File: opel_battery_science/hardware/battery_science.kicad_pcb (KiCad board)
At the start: 2 copper layers, 61 x 44.5 mm, 49 parts, among them P201 CONN_01X06, P301 CONN_01X08, P401 CONN_01X05, P402 CONN_01X05, Q301 BSS84, SW201 SPST, SW202 SPST, U201 LPC11C14, U301 BQ76925, U401 ADS1148IPWR

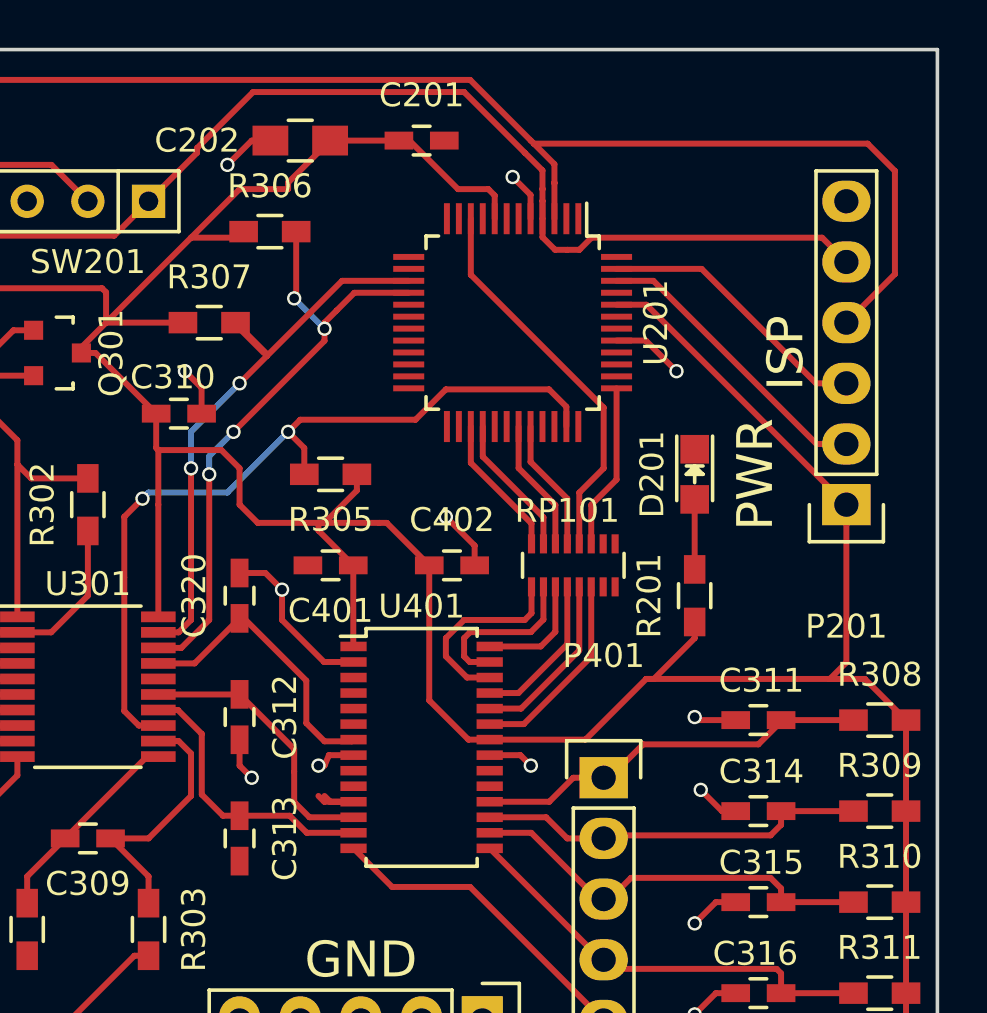
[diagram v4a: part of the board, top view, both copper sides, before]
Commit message: Moved input pins for ease of programming and avoiding accidental negative readings
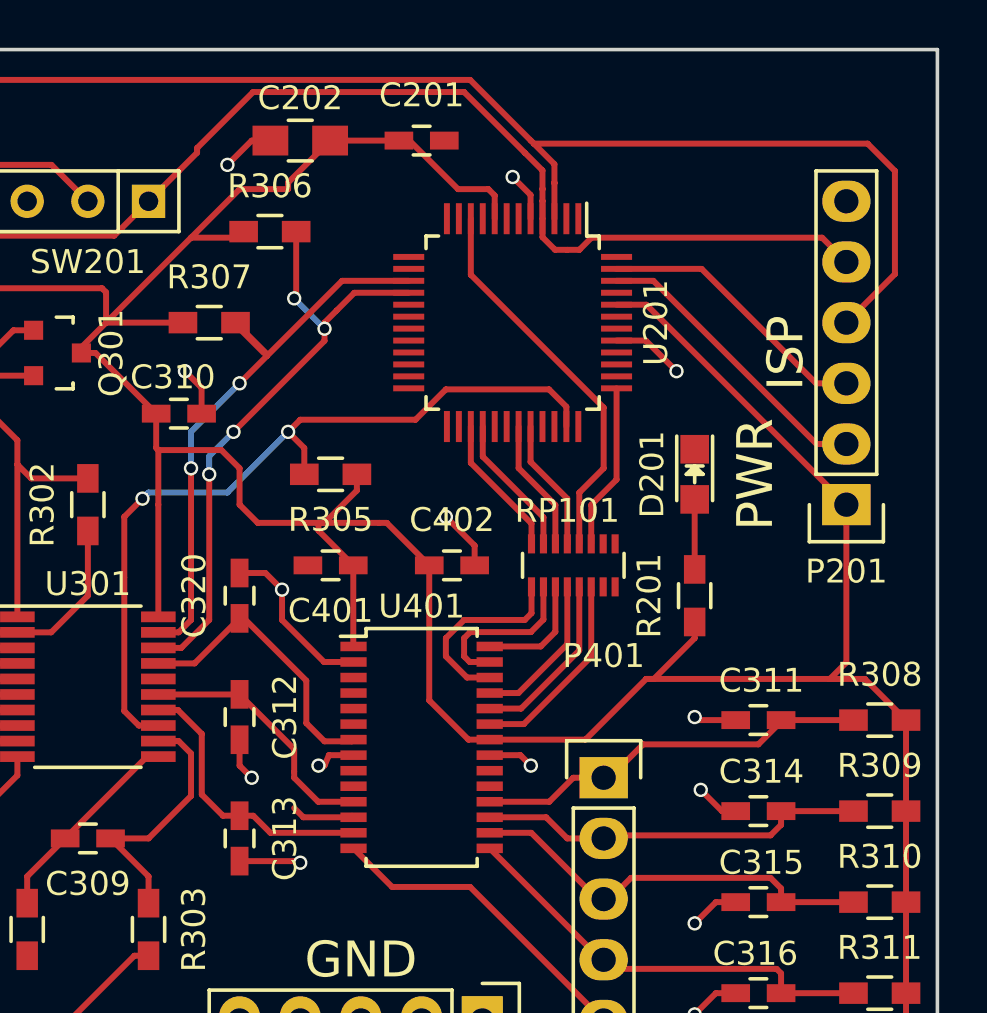
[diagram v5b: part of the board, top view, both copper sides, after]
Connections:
- U401 pad 11: GND -> /ADC/Thermistors/VCOUT
- U401 pad 12: /ADC/Thermistors/VCOUT -> GND
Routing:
- net GND: track 67.0 -> 69.4 mm, vias 24 -> 25
- net /ADC/Thermistors/VCOUT: track 11.7 -> 10.8 mm
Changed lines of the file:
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@@
     (thickness 1.6)
     (drawings 10)
-    (tracks 490)
+    (tracks 492)
     (zones 0)
     (modules 49)
@@
     (tags "capacitor 0805")
     (attr smd)
-    (fp_text reference C202 (at 4.318 0 180) (layer F.SilkS)
+    (fp_text reference C202 (at 0 1.778 180) (layer F.SilkS)
       (effects (font (size 1 1) (thickness 0.15)))
     )
@@
     (descr "Through hole pin header")
     (tags "pin header")
-    (fp_text reference P201 (at 0 -5.1 180) (layer F.SilkS)
+    (fp_text reference P201 (at 0 -2.794 180) (layer F.SilkS)
       (effects (font (size 1 1) (thickness 0.15)))
     )
@@
       (net 81 "Net-(U401-Pad10)"))
     (pad 11 smd rect (at -2.85 2.275) (size 1.1 0.4) (layers F.Cu F.Paste F.Mask)
-      (net 1 GND))
+      (net 21 /ADC/Thermistors/VCOUT))
     (pad 12 smd rect (at -2.85 2.925) (size 1.1 0.4) (layers F.Cu F.Paste F.Mask)
-      (net 21 /ADC/Thermistors/VCOUT))
+      (net 1 GND))
     (pad 13 smd rect (at -2.85 3.575) (size 1.1 0.4) (layers F.Cu F.Paste F.Mask)
       (net 22 /ADC/Thermistors/VIOUT))
@@
     (effects (font (size 1.5 1.5) (thickness 0.3)))
   )
-  (segment (start 158.44 129.275) (end 157.215 129.275) (width 0.25) (layer F.Cu) (net 1) (status 400000))
-  (segment (start 157.215 129.275) (end 156.972 129.032) (width 0.25) (layer F.Cu) (net 1))
-  (segment (start 158.44 129.275) (end 157.469 129.275) (width 0.25) (layer F.Cu) (net 1) (status 400000))
-  (segment (start 157.469 129.275) (end 157.226 129.032) (width 0.25) (layer F.Cu) (net 1))
+  (segment (start 158.44 129.925) (end 156.341 129.925) (width 0.25) (layer F.Cu) (net 1) (status 400000))
+  (segment (start 156.341 129.925) (end 155.956 129.54) (width 0.25) (layer F.Cu) (net 1))
+  (segment (start 153.67 131.76) (end 156.144 131.76) (width 0.25) (layer F.Cu) (net 1))
+  (via (at 156.21 131.826) (size 0.6) (drill 0.4) (layers F.Cu B.Cu) (net 1))
+  (segment (start 156.144 131.76) (end 156.21 131.826) (width 0.25) (layer F.Cu) (net 1))
   (segment (start 163.51 119.38) (end 163.51 118.552) (width 0.25) (layer F.Cu) (net 1))
   (via (at 162.306 117.348) (size 0.6) (drill 0.4) (layers F.Cu B.Cu) (net 1))
@@
   (segment (start 136.398 114.808) (end 135.382 114.808) (width 0.25) (layer F.Cu) (net 1))
   (segment (start 137.094 115.504) (end 136.398 114.808) (width 0.25) (layer F.Cu) (net 1))
+  (segment (start 158.375 129.86) (end 158.44 129.925) (width 0.25) (layer F.Cu) (net 1))
   (segment (start 161.61 119.38) (end 161.61 125.034) (width 0.25) (layer F.Cu) (net 2))
   (segment (start 163.251 126.675) (end 164.14 126.675) (width 0.25) (layer F.Cu) (net 2))
@@
   (segment (start 179.367 125.857) (end 176.337 125.857) (width 0.25) (layer F.Cu) (net 20))
   (segment (start 170.561 126.873) (end 169.037 128.397) (width 0.25) (layer F.Cu) (net 20))
-  (segment (start 155.956 128.016) (end 155.956 129.286) (width 0.25) (layer F.Cu) (net 21))
+  (segment (start 155.956 128.016) (end 155.956 128.27) (width 0.25) (layer F.Cu) (net 21))
+  (segment (start 153.67 124.78) (end 155.956 127.066) (width 0.25) (layer F.Cu) (net 21))
   (segment (start 155.956 128.016) (end 155.956 127.066) (width 0.25) (layer F.Cu) (net 21))
-  (segment (start 153.67 124.78) (end 155.956 127.066) (width 0.25) (layer F.Cu) (net 21))
-  (segment (start 156.595 129.925) (end 158.44 129.925) (width 0.25) (layer F.Cu) (net 21) (status 800000))
-  (segment (start 155.956 129.286) (end 156.595 129.925) (width 0.25) (layer F.Cu) (net 21))
+  (segment (start 156.961 129.275) (end 158.44 129.275) (width 0.25) (layer F.Cu) (net 21))
+  (segment (start 155.956 128.27) (end 156.961 129.275) (width 0.25) (layer F.Cu) (net 21))
   (segment (start 150.27 124.785) (end 153.741 124.785) (width 0.25) (layer F.Cu) (net 21))
-  (segment (start 153.67 129.86) (end 155.768 129.86) (width 0.25) (layer F.Cu) (net 22))
-  (segment (start 156.483 130.575) (end 158.44 130.575) (width 0.25) (layer F.Cu) (net 22))
-  (segment (start 155.768 129.86) (end 156.483 130.575) (width 0.25) (layer F.Cu) (net 22))
+  (segment (start 153.67 129.86) (end 154.244 129.86) (width 0.25) (layer F.Cu) (net 22) (status 400000))
+  (segment (start 154.959 130.575) (end 158.44 130.575) (width 0.25) (layer F.Cu) (net 22) (status 800000))
+  (segment (start 154.244 129.86) (end 154.959 130.575) (width 0.25) (layer F.Cu) (net 22))
   (segment (start 150.27 125.435) (end 151.089 125.435) (width 0.25) (layer F.Cu) (net 22))
   (segment (start 152.974 129.86) (end 153.67 129.86) (width 0.25) (layer F.Cu) (net 22))
